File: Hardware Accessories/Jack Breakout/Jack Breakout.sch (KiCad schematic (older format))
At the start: 3 parts, among them J1 AudioJack3_Switch, J2 Conn_01x03

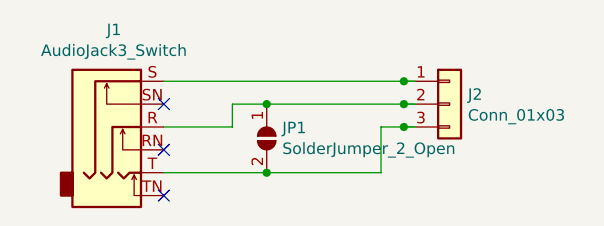
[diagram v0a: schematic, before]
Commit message: Fixed jack breakout misalignment
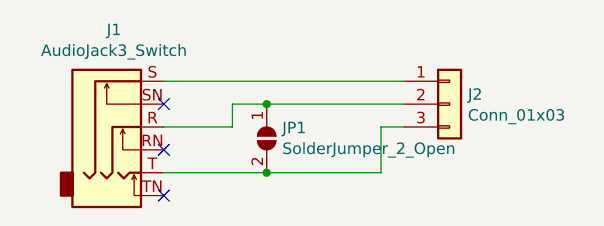
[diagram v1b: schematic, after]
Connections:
- wire segments 12 -> 9
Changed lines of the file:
@@
-$EndComp
-$Comp
-L Connector_Generic:Conn_01x03 J2
-U 1 1 5E4D8113
-P 3150 1200
-F 0 "J2" H 3230 1242 50  0000 L CNN
-F 1 "Conn_01x03" H 3230 1151 50  0000 L CNN
-F 2 "Connector_Molex:Molex_KK-254_AE-6410-03A_1x03_P2.54mm_Vertical" H 3150 1200 50  0001 C CNN
-F 3 "~" H 3150 1200 50  0001 C CNN
-	1    3150 1200
-	1    0    0    -1
 $EndComp
 $Comp
@@
 NoConn ~ 1900 1200
 Wire Wire Line
-	1900 1100 2950 1100
+	2350 1500 2850 1500
+Wire Wire Line
+	2850 1500 2850 1300
+Connection ~ 2350 1500
+$Comp
+L Connector_Generic:Conn_01x03 J2
+U 1 1 5E4D8113
+P 3150 1200
+F 0 "J2" H 3230 1242 50  0000 L CNN
+F 1 "Conn_01x03" H 3230 1151 50  0000 L CNN
+F 2 "Connector_Molex:Molex_KK-254_AE-6410-03A_1x03_P2.54mm_Vertical" H 3150 1200 50  0001 C CNN
+F 3 "~" H 3150 1200 50  0001 C CNN
+	1    3150 1200
+	1    0    0    -1
+$EndComp
+Wire Wire Line
+	2950 1100 1900 1100
 Wire Wire Line
 	2350 1200 2950 1200
 Connection ~ 2350 1200
 Wire Wire Line
-	2350 1500 2850 1500
-Wire Wire Line
-	2850 1500 2850 1300
-Wire Wire Line
 	2850 1300 2950 1300
-Connection ~ 2350 1500
-Connection ~ 2950 1100
-Wire Wire Line
-	2950 1100 3000 1100
-Connection ~ 2950 1200
-Wire Wire Line
-	2950 1200 3000 1200
-Connection ~ 2950 1300
-Wire Wire Line
-	2950 1300 3000 1300
 $EndSCHEMATC
